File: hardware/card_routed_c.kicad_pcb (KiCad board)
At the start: 2 copper layers, 143 x 80 mm, 1 part

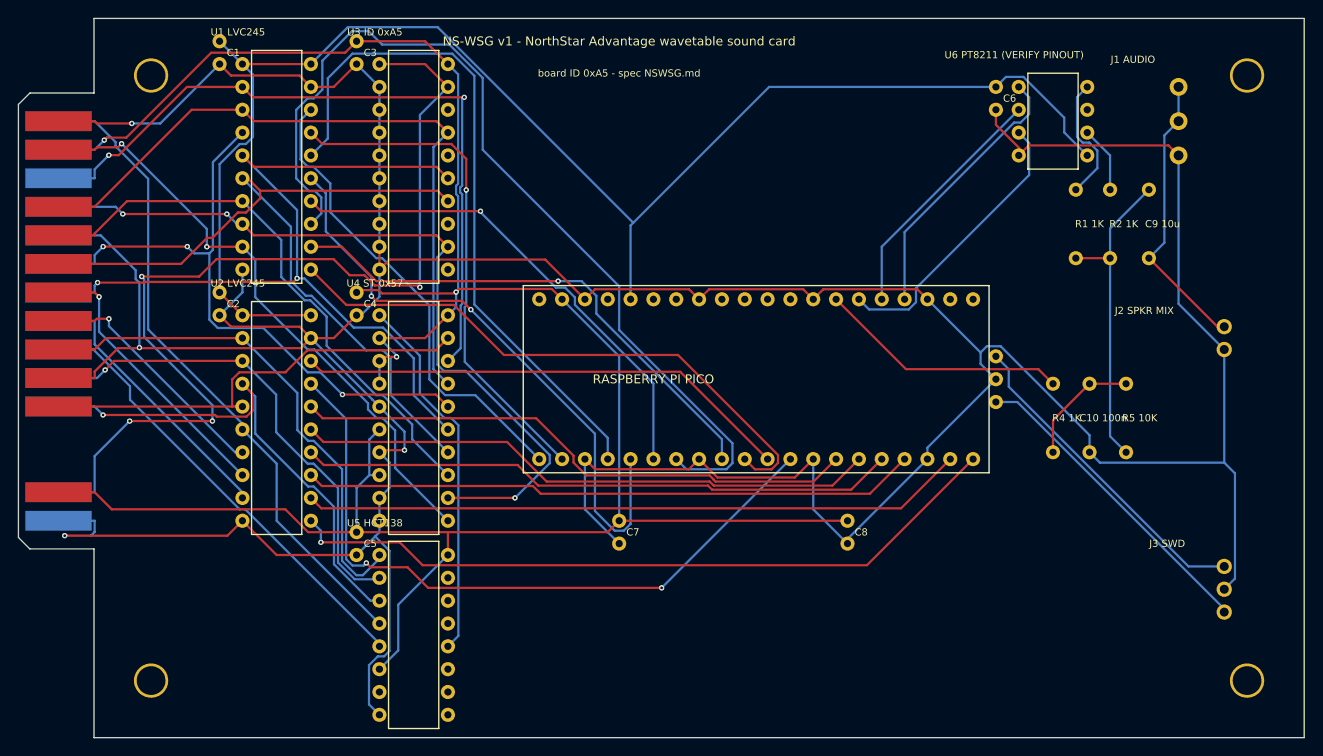
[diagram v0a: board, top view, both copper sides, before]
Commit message: Rebase card on Raspberry Pi Pico W (socketed) with antenna keep-out
The W is pin-compatible, so the change is layout hygiene: removed the
board-level SWD pads and J3 (the Pico WH carries its own JST-SH debug
connector), added a rule-area keep-out under the antenna end (no vias,
no future copper pour; verified 0 vias inside, only pins 19-22 escapes
cross), ANTENNA silk marking, and module socketing noted. Re-routed:
freerouting 999.99, KiCad DRC 0 violations / 0 unconnected. Fab
package and 1:1 plots regenerated. WiFi buys OTA firmware updates and
a live synth-state web view now; the v2 readable-port extension turns
it into a network pipe later.

Co-Authored-By: Claude Fable 5 <noreply@anthropic.com>
Claude-Session: https://claude.ai/code/session_01PB6zhL6oFB9zbtD4W85UDt
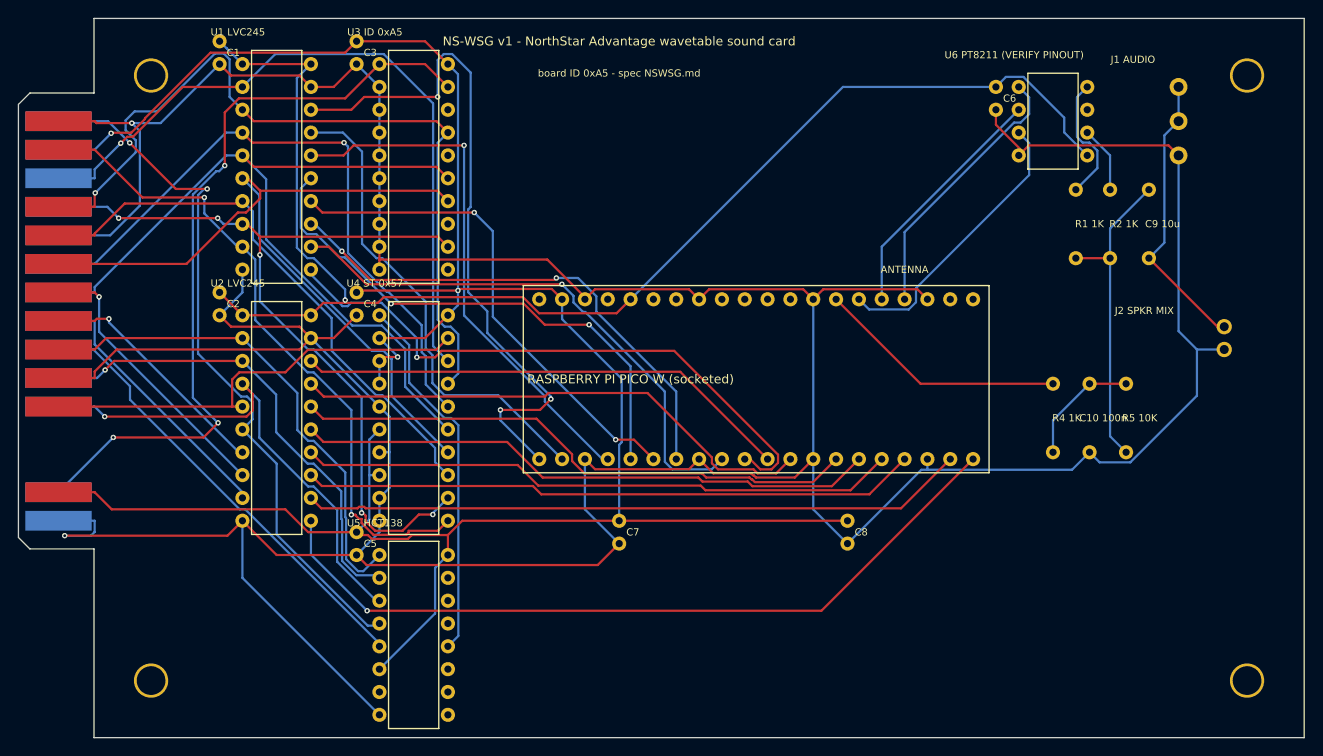
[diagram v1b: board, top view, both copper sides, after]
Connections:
- ? pad 169: SWCLK -> AOL
- ? pad 170: GND -> ASUM
- ? pad 171: SWDIO -> AOR
- ? pad 172: AOL -> ASUM
- ? pad 174: AOR -> AOUT
- ? pad 175: ASUM -> PWM
- ? pad 176: ASUM -> PWMF
- ? pad 177: AOUT -> PWMF
- ? pad 178: PWM -> GND
- ? pad 180: PWMF -> ASUM
- ? pad 181: GND -> AOUT
- ? pad 182: PWMF -> AOUT
- ? pad 183: ASUM -> GND
- ? pad 185: AOUT -> GND
- ? pad 186: GND -> +3V3
- ? pad 187: AOUT -> GND
- ? pad 188: GND -> +3V3
- ? pad 189: SWCLK -> GND
- ? pad 190: GND -> +5V
- ? pad 191: SWDIO -> GND
- ? pad 192: +3V3 -> +5V
- ? pad 194: +3V3 -> +5V
- ? pad 196: +5V -> +3V3
- ? pad 202: +3V3 -> (no net)
- ? pad 203: GND -> (no net)
- ? pad 204: +5V -> (no net)
- ? pad 205: GND -> (no net)
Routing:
- net GP5: track 104.5 -> 57.1 mm, vias 0 -> 2
- net SWCLK: track 36.2 -> 0.00 mm
- net SWDIO: track 35.3 -> 0.00 mm
- net GP0: track 53.1 -> 77.2 mm, vias 0 -> 3
- net IDREQ: track 107.4 -> 86.4 mm, vias 4 -> 3
- net GP9: track 78.1 -> 58.8 mm, vias 2 -> 0
- net GP2: track 76.6 -> 59.4 mm, vias 0 -> 1
- net IO1: track 78.1 -> 91.3 mm, vias 0 -> 1
- net +3V3: track 167.3 -> 155.7 mm, vias 0 -> 1
- net GP3: track 68.1 -> 59.4 mm
- net IO7: track 67.4 -> 73.9 mm
- net SEL: track 73.0 -> 79.4 mm, vias 0 -> 2
- net GP15: track 81.4 -> 87.0 mm
- net IO6: track 89.2 -> 93.3 mm, vias 3 -> 5
- net GP6: track 58.0 -> 61.5 mm
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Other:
- board text added: "ANTENNA"
- board text added: "RASPBERRY PI PICO W (socketed)"
- board text removed: "J3 SWD"
- board text removed: "RASPBERRY PI PICO"

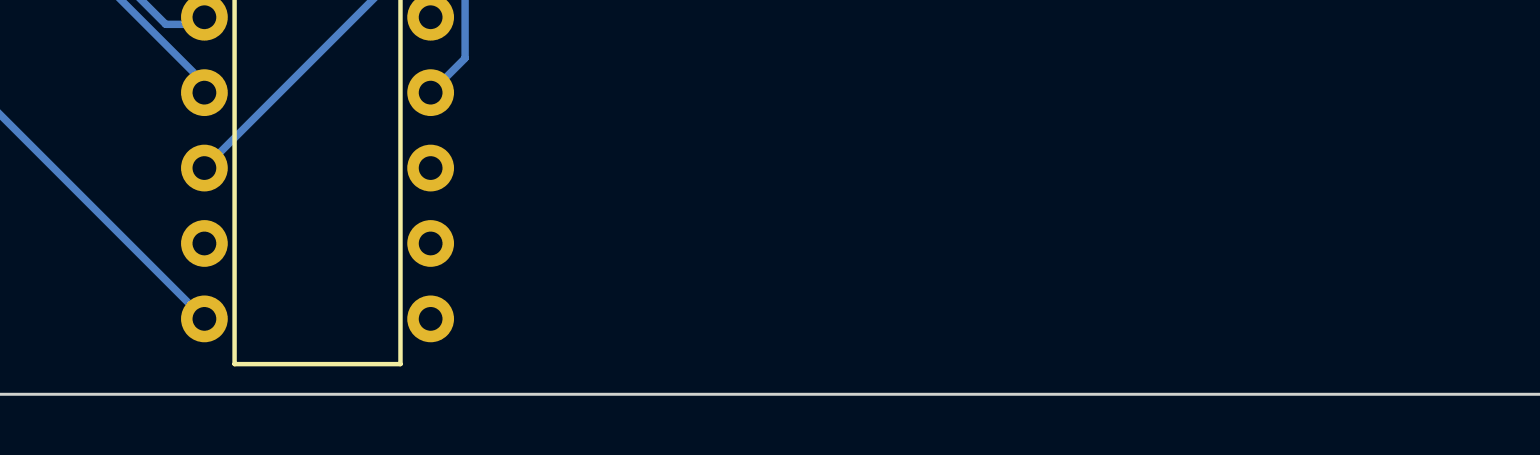
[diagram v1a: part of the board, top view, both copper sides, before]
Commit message: Order prep: memorial notice on both boards, ORDER.md package
Both boards now carry "(c) 2026 David Troy, in memory of Stephen
Troy." on the silkscreen — the card along its bottom edge, the riser
on two lines. Regenerated boards, fab zips, gerbers, and 1:1 plots;
re-verified DRC-clean (0 violations, 0 unconnected on both). ORDER.md
carries the full PCBWay parameter set, the pre-upload checklist, the
per-card BOM, and the bring-up sequence for when the boards arrive.

Co-Authored-By: Claude Fable 5 <noreply@anthropic.com>
Claude-Session: https://claude.ai/code/session_01PB6zhL6oFB9zbtD4W85UDt
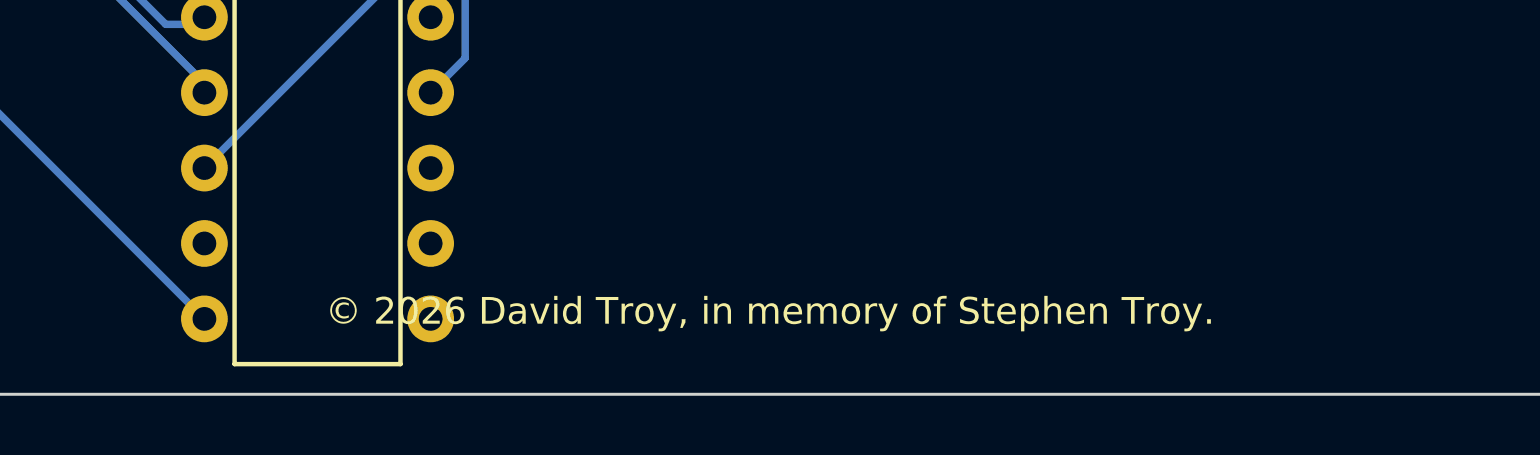
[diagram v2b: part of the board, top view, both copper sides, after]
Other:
- board text added: "© 2026 David Troy, in memory of Stephen Troy."
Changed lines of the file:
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@@
   (gr_text "NS-WSG v1 - NorthStar Advantage wavetable sound card" (at 143.4200 67.5400) (layer "F.SilkS") (effects (font (size 1.0 1.0) (thickness 0.15))))
   (gr_text "board ID 0xA5 - spec NSWSG.md" (at 143.4200 71.0960) (layer "F.SilkS") (effects (font (size 0.8 0.8) (thickness 0.15))))
+  (gr_text "© 2026 David Troy, in memory of Stephen Troy." (at 135.8000 142.2160) (layer "F.SilkS") (effects (font (size 0.9 0.9) (thickness 0.15))))
   (segment (start 139.6100 96.2420) (end 139.6100 96.0120) (width 0.25) (layer "F.Cu") (net 1))
   (segment (start 139.6100 96.0120) (end 135.4219 91.8239) (width 0.25) (layer "F.Cu") (net 1))

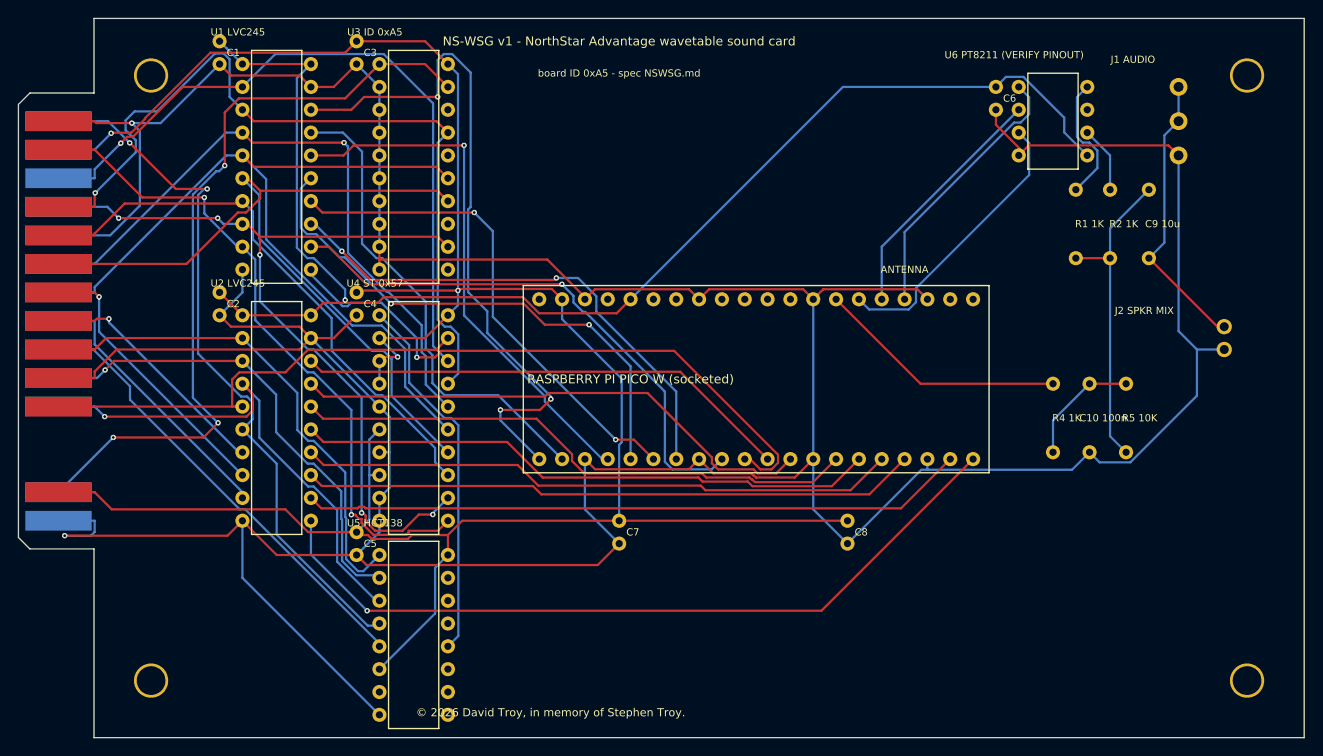
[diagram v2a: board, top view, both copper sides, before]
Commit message: Pre-fab footprint audit: J1 becomes a header, U6 package flagged
Audited every footprint before the order. All standard 0.1"
through-hole except J1, which was an invented 3-pad "jack" matching no
real part — replaced with a plain 1x3 header (pigtail to a panel jack;
real TRS footprint is v2, chosen from a datasheet). U6 check upgraded
to pinout AND package (PT8211 is often SOP-8; adapter-in-socket
fallback documented). Re-routed and re-verified: 0 violations, 0
unconnected. ORDER.md carries the audit results.

Co-Authored-By: Claude Fable 5 <noreply@anthropic.com>
Claude-Session: https://claude.ai/code/session_01PB6zhL6oFB9zbtD4W85UDt
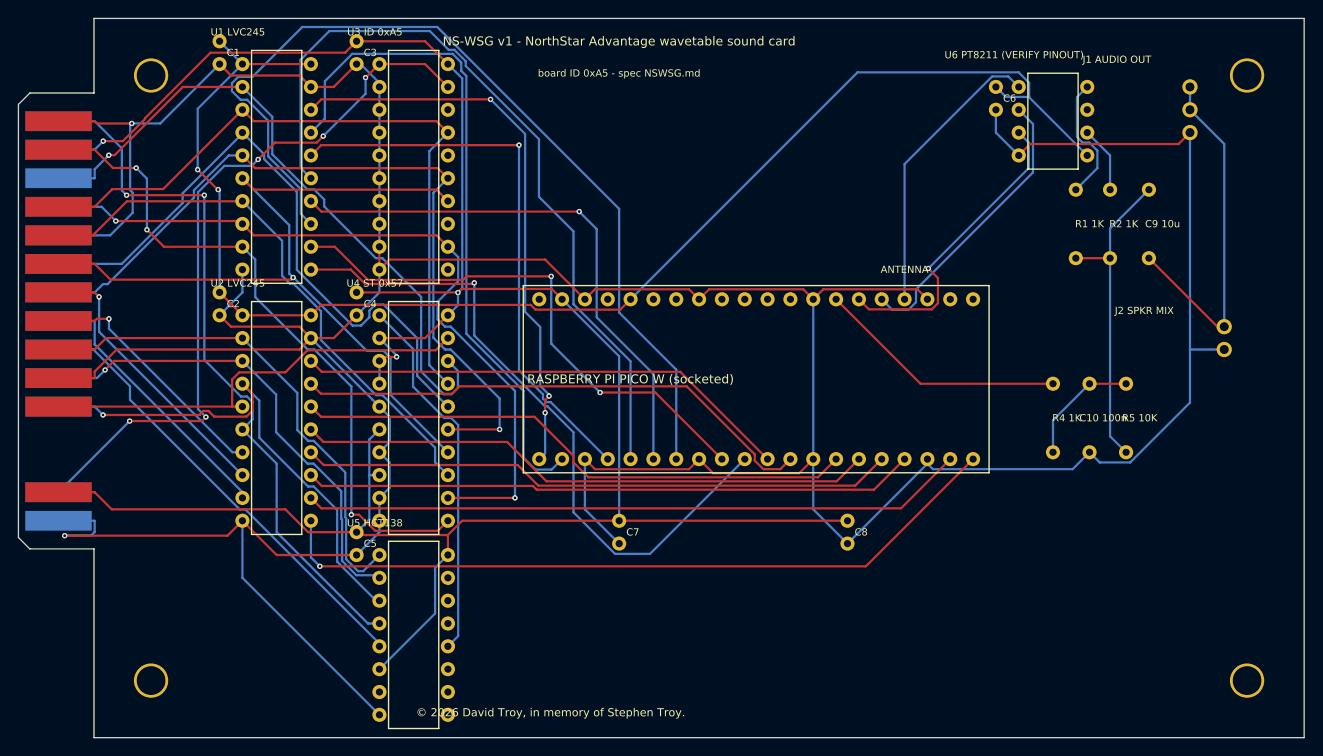
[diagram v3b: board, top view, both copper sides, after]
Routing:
- net GP5: track 57.1 -> 104.2 mm, vias 2 -> 0
- net GP3: track 59.4 -> 86.6 mm, vias 2 -> 0
- net GP1: track 53.9 -> 75.3 mm
- net GND: track 504.7 -> 483.3 mm
- net GP0: track 77.2 -> 63.6 mm
- net IO1: track 91.3 -> 78.5 mm, vias 1 -> 0
- net AOUT: track 32.0 -> 39.8 mm
- net IO6: track 93.3 -> 85.9 mm, vias 5 -> 2
- net GP7: track 68.4 -> 74.5 mm
- net GP4: track 55.6 -> 61.3 mm, vias 2 -> 1
- net IDREQ: track 86.4 -> 81.0 mm, vias 3 -> 5
- net WS: track 27.4 -> 32.1 mm
- net IO0: track 79.6 -> 74.9 mm
- net IO3: track 92.9 -> 89.0 mm, vias 0 -> 1
- net GP15: track 87.0 -> 83.1 mm
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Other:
- board text added: "J1 AUDIO OUT"
- board text removed: "J1 AUDIO"

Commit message: U6 dual position: SOP-8 land beside the DIP socket
PT8211's standard package is SOP-8 (user-confirmed). Nesting SOIC pads
inside the DIP rows failed DRC (6mm cavity is too tight for honest
lands), so U6B is a full-size SOP-8 land beside the DIP position on
the same nets — populate one. Also: injector nudges freerouting's
rare near-min neckdowns (0.15-0.2mm) up to the 0.2mm floor. DRC: 0
violations, 0 unconnected. ORDER.md documents the dual position and
the audio-output options (line-level J1, amp needed for bare 8-ohm
speakers, J2 mix-in for the machine's own speaker).

Co-Authored-By: Claude Fable 5 <noreply@anthropic.com>
Claude-Session: https://claude.ai/code/session_01PB6zhL6oFB9zbtD4W85UDt
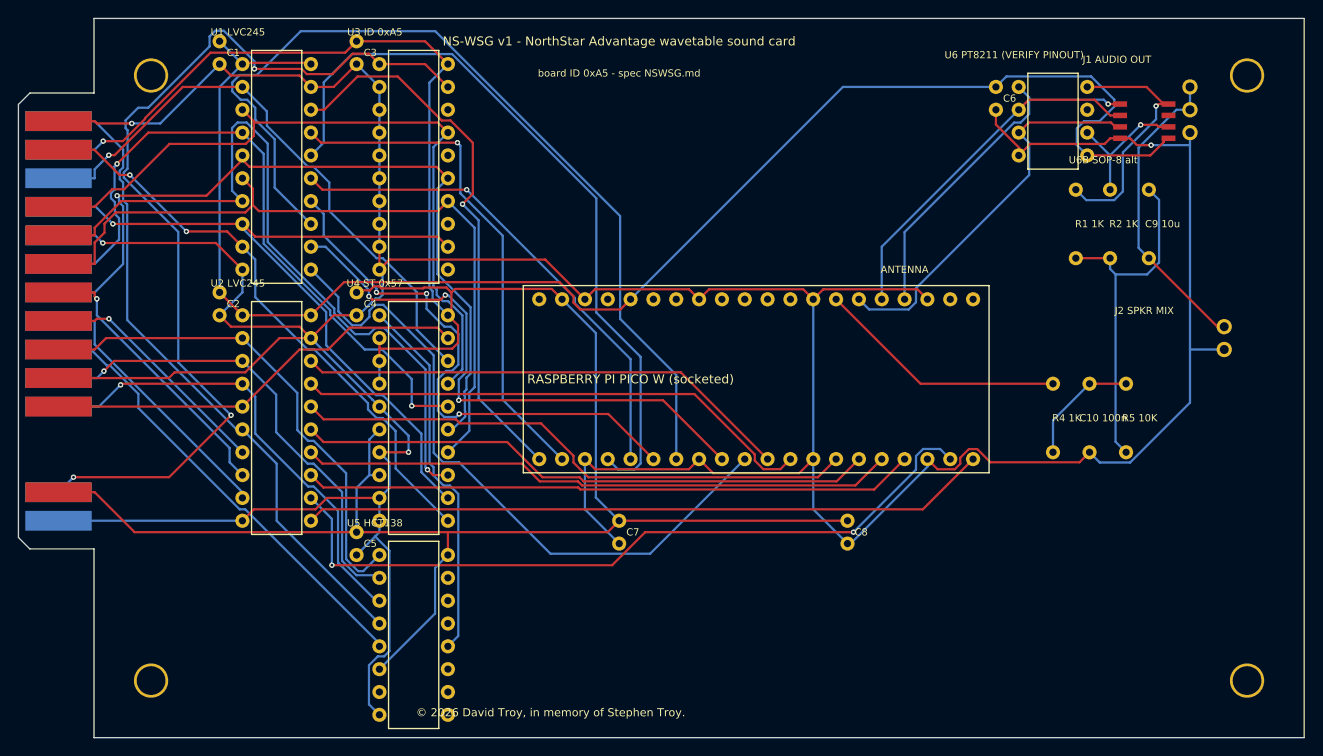
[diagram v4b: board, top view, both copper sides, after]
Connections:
- ? pad 129: GP0 -> BCK
- ? pad 130: (no net) -> AOL
- ? pad 131: GP1 -> WS
- ? pad 132: +5V -> (no net)
- ? pad 133: GND -> DIN
- ? pad 134: GND -> AOR
- ? pad 135: GP2 -> GND
- ? pad 136: (no net) -> +3V3
- ? pad 137: GP3 -> GP0
- ? pad 138: +3V3 -> (no net)
- ? pad 139: GP4 -> GP1
- ? pad 140: (no net) -> +5V
- ? pad 141: GP5 -> GND
- ? pad 142: (no net) -> GND
- ? pad 143: GND -> GP2
- ? pad 144: GND -> (no net)
- ? pad 145: GP6 -> GP3
- ? pad 146: (no net) -> +3V3
- ? pad 147: GP7 -> GP4
- ? pad 149: GP8 -> GP5
- ? pad 151: GP9 -> GND
- ? pad 152: (no net) -> GND
- ? pad 153: GND -> GP6
- ? pad 154: GND -> (no net)
- ? pad 155: GP10 -> GP7
- ? pad 156: PWM -> (no net)
- ? pad 157: GP11 -> GP8
- ? pad 158: DIN -> (no net)
- ? pad 159: GP12 -> GP9
- ? pad 160: WS -> (no net)
- ? pad 161: GP13 -> GND
- ? pad 162: BCK -> GND
- ? pad 163: GND -> GP10
- ? pad 164: GND -> PWM
- ? pad 165: GP14 -> GP11
- ? pad 166: (no net) -> DIN
- ? pad 167: GP15 -> GP12
- ? pad 168: (no net) -> WS
- ? pad 169: AOL -> GP13
- ? pad 170: ASUM -> BCK
- ? pad 171: AOR -> GND
- ? pad 172: ASUM -> GND
- ? pad 173: ASUM -> GP14
- ? pad 174: AOUT -> (no net)
- ? pad 175: PWM -> GP15
- ? pad 176: PWMF -> (no net)
- ? pad 177: PWMF -> AOL
- ? pad 178: GND -> ASUM
- ? pad 179: PWMF -> AOR
- ? pad 181: AOUT -> ASUM
- ? pad 183: GND -> PWM
- ? pad 184: AOUT -> PWMF
- ? pad 185: GND -> PWMF
- ? pad 186: +3V3 -> GND
- ? pad 187: GND -> PWMF
- ? pad 188: +3V3 -> ASUM
- ? pad 189: GND -> AOUT
- ? pad 190: +5V -> AOUT
- ? pad 192: +5V -> AOUT
- ? pad 194: +5V -> +3V3
- ? pad 202: (no net) -> +5V
- ? pad 203: (no net) -> GND
- ? pad 204: (no net) -> +3V3
- ? pad 205: (no net) -> GND
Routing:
- net GP3: track 86.6 -> 55.4 mm, vias 0 -> 1
- net IDREQ: track 81.0 -> 106.3 mm, vias 5 -> 3
- net IO5: track 62.8 -> 85.3 mm, vias 0 -> 1
- net GP2: track 62.9 -> 82.9 mm, vias 1 -> 0
- net GP1: track 75.3 -> 56.8 mm, vias 0 -> 1
- net +3V3: track 157.9 -> 172.9 mm, vias 2 -> 0
- net AOL: track 14.3 -> 27.9 mm, vias 0 -> 1
- net GP14: track 73.9 -> 83.9 mm, vias 0 -> 2
- net IO7: track 75.5 -> 65.7 mm, vias 3 -> 2
- net DIN: track 34.1 -> 43.7 mm, vias 1 -> 0
- net IO4: track 91.9 -> 82.7 mm, vias 1 -> 0
- net IO0: track 74.9 -> 66.0 mm
- net BCK: track 32.3 -> 40.6 mm, vias 0 -> 1
- net AOR: track 7.40 -> 15.4 mm, vias 0 -> 1
- net WS: track 32.1 -> 39.9 mm
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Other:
- board text added: "U6B SOP-8 alt"
